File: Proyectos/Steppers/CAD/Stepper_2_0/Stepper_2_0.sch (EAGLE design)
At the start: 4 parts

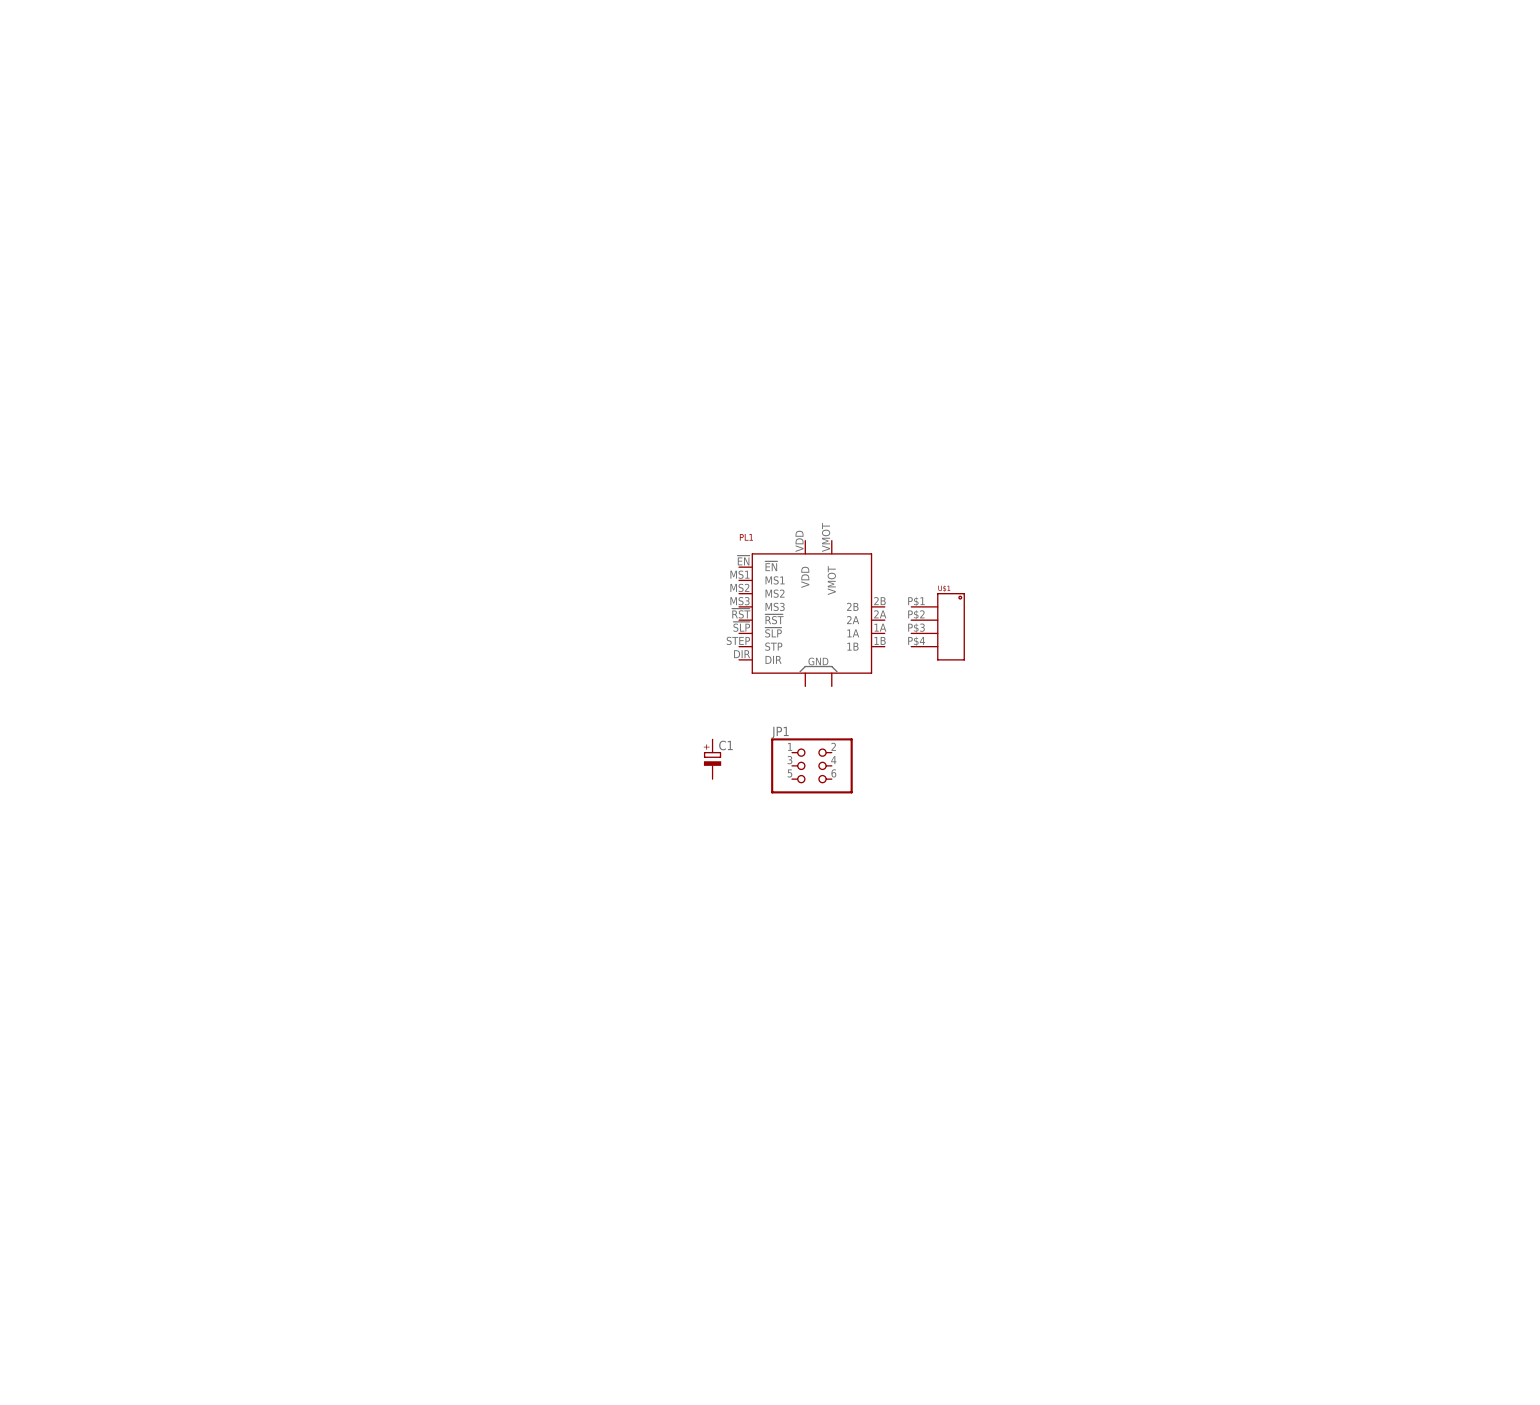
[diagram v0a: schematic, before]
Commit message: Steppers:
Se comienza a agregar el potenciómetro a lalibreria del proyecto, se avanza con el esquemático dela V2
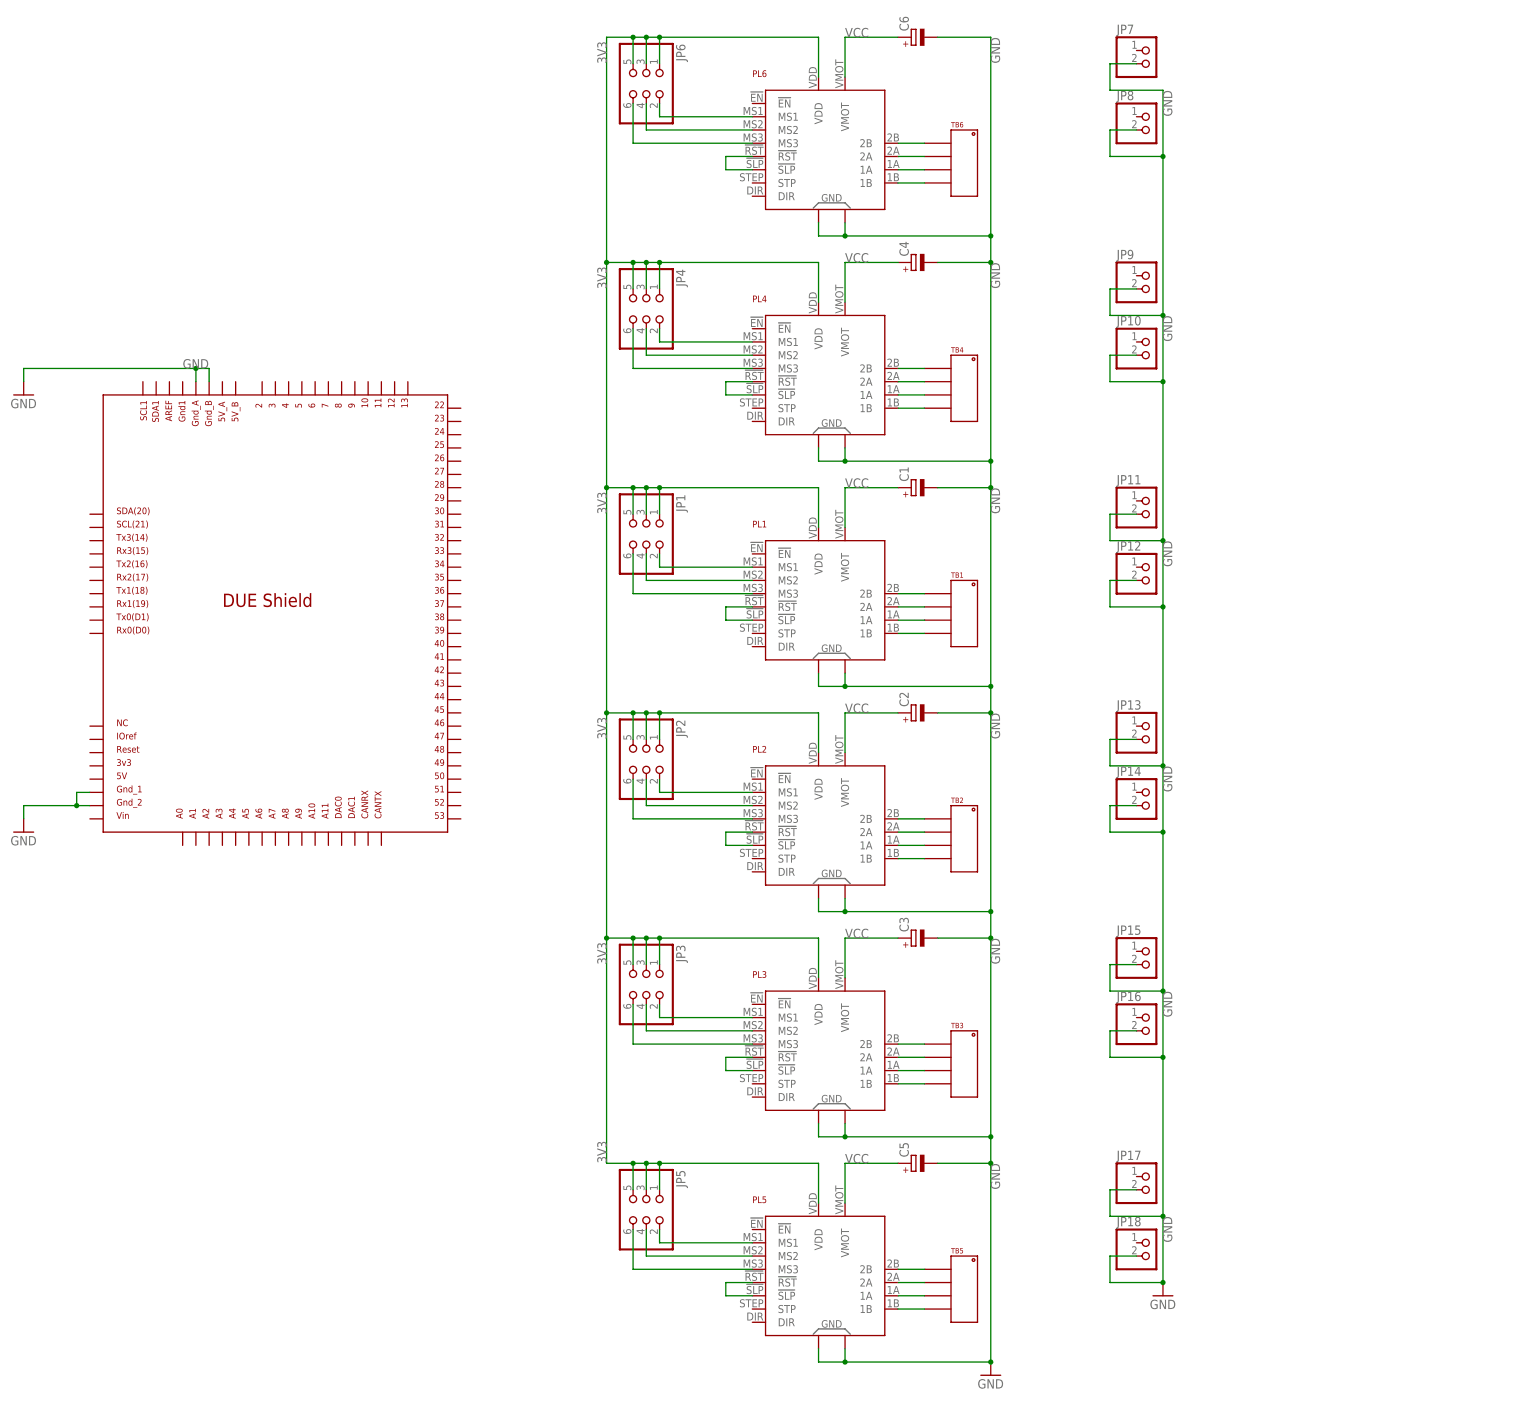
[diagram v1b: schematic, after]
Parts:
- added C2, C3, C4, C5, C6: (no value), rcl:CPOL-EUETR2
- added JP10, JP11, JP12, JP13, JP14, JP15, JP16, JP17, JP18, JP7, JP8, JP9: (no value), pinhead:PINHD-1X2
- added JP2, JP3, JP4, JP5, JP6: (no value), pinhead:PINHD-2X3
- added PL2, PL3, PL4, PL5, PL6: A4988X, Steppers:A4988X
- added TB1, TB2, TB3, TB4, TB5, TB6: TB_HEAD_3.5MM_01X04, Steppers:TB_HEAD_3.5MM_01X04
- U$1: value TB_HEAD_3.5MM_01X04 -> DUE(NOSPI); device Steppers:TB_HEAD_3.5MM_01X04 -> JoshParts:DUE(NOSPI)
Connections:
- new net 3V3: JP1.1, JP1.3, JP1.5, JP2.1, JP2.3, JP2.5, JP3.1, JP3.3, JP3.5, JP4.1, JP4.3, JP4.5, JP5.1, JP5.3, JP5.5, JP6.1, JP6.3, JP6.5, PL1.VDD, PL2.VDD, PL3.VDD, PL4.VDD, PL5.VDD, PL6.VDD
- new net GND: C1.-, C2.-, C3.-, C4.-, C5.-, C6.-, JP10.2, JP11.2, JP12.2, JP13.2, JP14.2, JP15.2, JP16.2, JP17.2, JP18.2, JP7.2, JP8.2, JP9.2, PL1.GND1, PL1.GND2, PL2.GND1, PL2.GND2, PL3.GND1, PL3.GND2, PL4.GND1, PL4.GND2, PL5.GND1, PL5.GND2, PL6.GND1, PL6.GND2, U$1.GND_1, U$1.GND_2, U$1.GND_A, U$1.GND_B
- new net N$1: PL1.1B, TB1.P$4
- new net N$11: PL1.!RST, PL1.!SLP
- new net N$13: PL2.1B, TB2.P$4
- new net N$14: PL2.1A, TB2.P$3
- new net N$15: PL2.2A, TB2.P$2
- new net N$16: PL2.2B, TB2.P$1
- new net N$18: PL2.!RST, PL2.!SLP
- new net N$2: PL1.1A, TB1.P$3
- new net N$20: JP2.6, PL2.MS3
- new net N$21: JP2.4, PL2.MS2
- new net N$22: JP2.2, PL2.MS1
- new net N$24: PL3.1B, TB3.P$4
- new net N$25: PL3.1A, TB3.P$3
- new net N$26: PL3.2A, TB3.P$2
- new net N$27: PL3.2B, TB3.P$1
- new net N$29: PL3.!RST, PL3.!SLP
- new net N$3: PL1.2A, TB1.P$2
- new net N$31: JP3.6, PL3.MS3
- new net N$32: JP3.4, PL3.MS2
- new net N$33: JP3.2, PL3.MS1
- new net N$35: PL4.1B, TB4.P$4
- new net N$36: PL4.1A, TB4.P$3
- new net N$37: PL4.2A, TB4.P$2
- new net N$38: PL4.2B, TB4.P$1
- new net N$4: PL1.2B, TB1.P$1
- new net N$40: PL4.!RST, PL4.!SLP
- new net N$42: JP4.6, PL4.MS3
- new net N$43: JP4.4, PL4.MS2
- new net N$44: JP4.2, PL4.MS1
- new net N$46: PL5.1B, TB5.P$4
- new net N$47: PL5.1A, TB5.P$3
- new net N$48: PL5.2A, TB5.P$2
- new net N$49: PL5.2B, TB5.P$1
- new net N$5: JP1.6, PL1.MS3
- new net N$51: PL5.!RST, PL5.!SLP
- new net N$53: JP5.6, PL5.MS3
- new net N$54: JP5.4, PL5.MS2
- new net N$55: JP5.2, PL5.MS1
- new net N$57: PL6.1B, TB6.P$4
- new net N$58: PL6.1A, TB6.P$3
- new net N$59: PL6.2A, TB6.P$2
- new net N$6: JP1.4, PL1.MS2
- new net N$60: PL6.2B, TB6.P$1
- new net N$62: PL6.!RST, PL6.!SLP
- new net N$64: JP6.6, PL6.MS3
- new net N$65: JP6.4, PL6.MS2
- new net N$66: JP6.2, PL6.MS1
- new net N$7: JP1.2, PL1.MS1
- new net VCC: C1.+, C2.+, C3.+, C4.+, C5.+, C6.+, PL1.VMOT, PL2.VMOT, PL3.VMOT, PL4.VMOT, PL5.VMOT, PL6.VMOT
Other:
- moved on the sheet: C1, JP1, PL1

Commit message: Steppers:
Se mejora el modelo del potenciómetro en la libreria y se agrega l boton de 6mm, se avanza en el esquemático de la V2
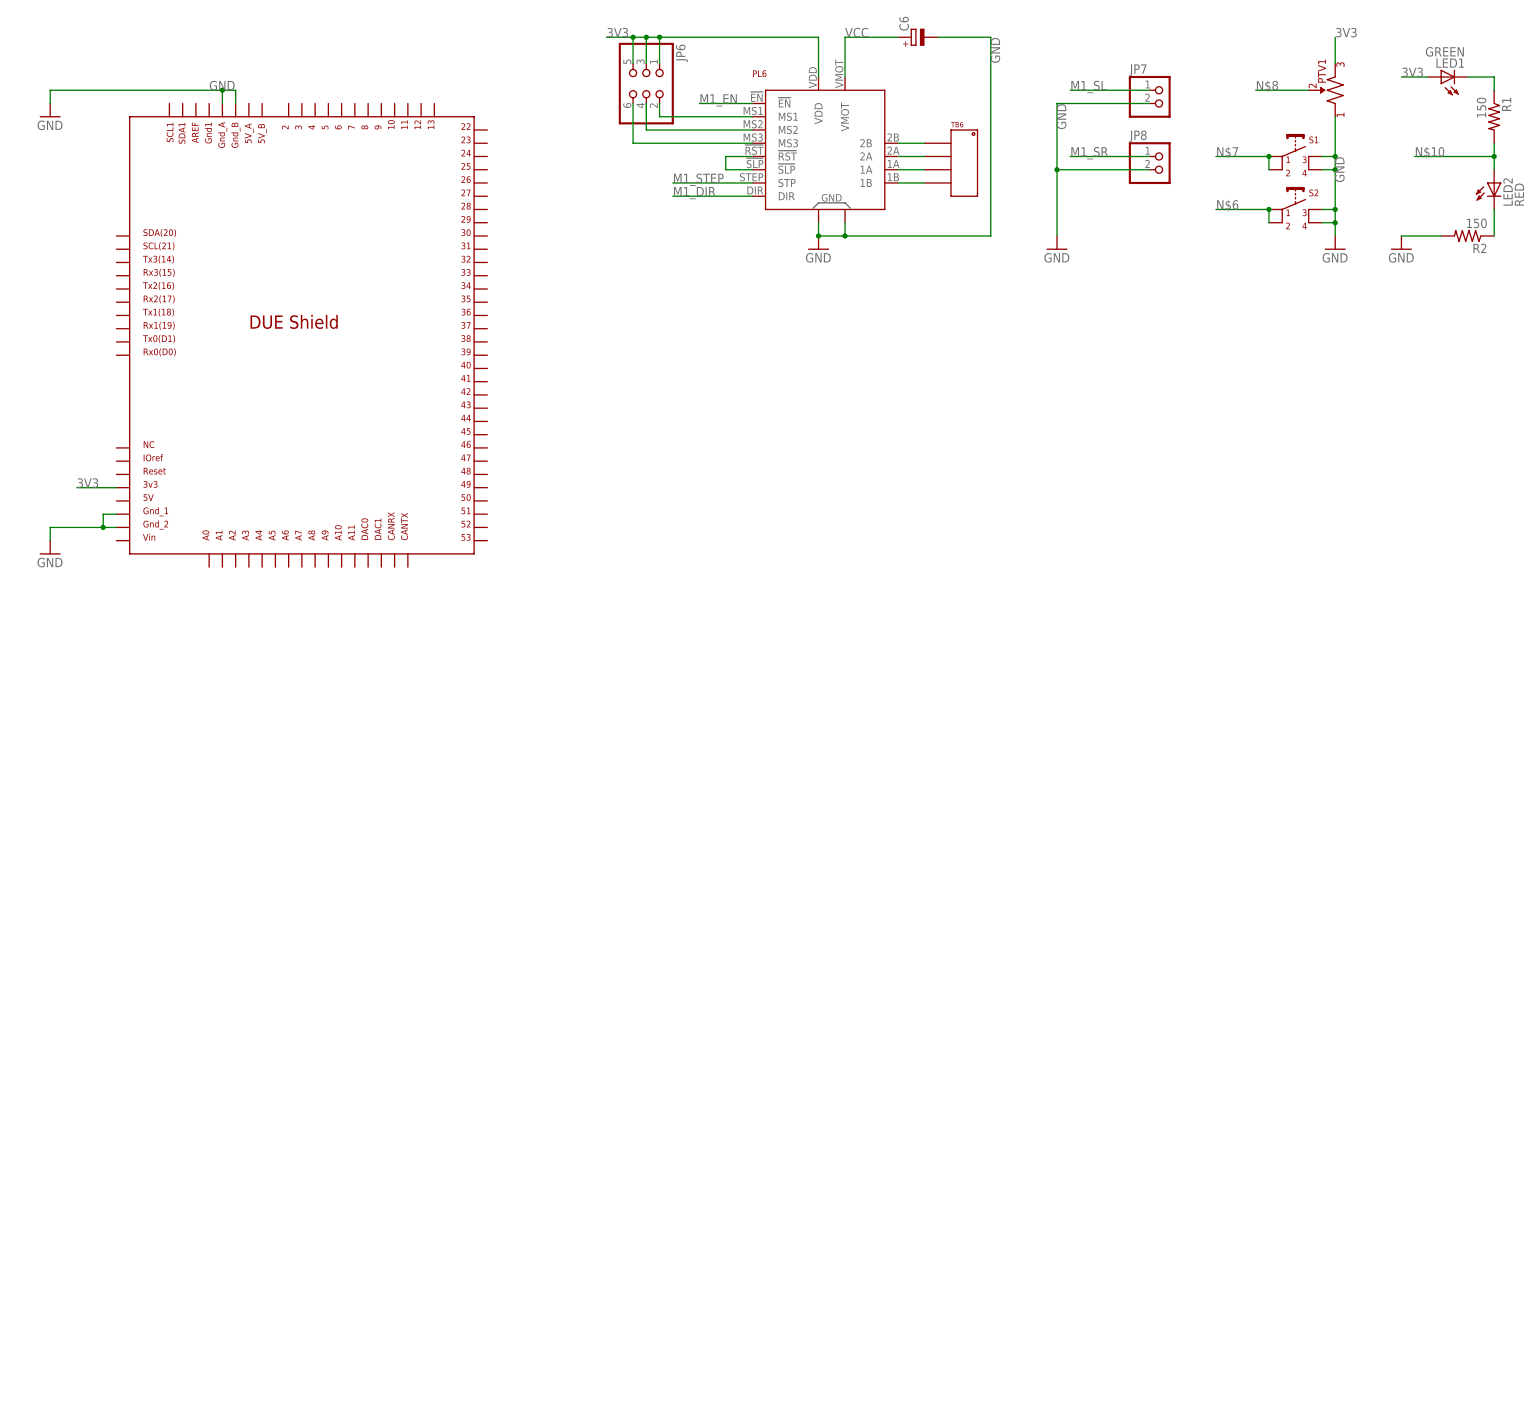
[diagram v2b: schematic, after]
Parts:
- removed C1, C2, C3, C4, C5: (no value), rcl:CPOL-EUETR2
- removed JP1, JP2, JP3, JP4, JP5: (no value), pinhead:PINHD-2X3
- removed JP10, JP11, JP12, JP13, JP14, JP15, JP16, JP17, JP18, JP9: (no value), pinhead:PINHD-1X2
- removed PL1, PL2, PL3, PL4, PL5: A4988X, Steppers:A4988X
- removed TB1, TB2, TB3, TB4, TB5: TB_HEAD_3.5MM_01X04, Steppers:TB_HEAD_3.5MM_01X04
- added LED1: GREEN, adafruit:LEDSMT1206
- added LED2: RED, adafruit:LEDSMT1206
- added PTV1: PTV09A-4, Steppers:PTV09A-4
- added R1, R2: 150, SparkFun-Resistors:RESISTOR1206
- added S1, S2: BTN_SPST_6MM, Steppers:BTN_SPST_6MM
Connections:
- removed net N$1: PL1.1B, TB1.P$4
- removed net N$13: PL2.1B, TB2.P$4
- removed net N$14: PL2.1A, TB2.P$3
- removed net N$15: PL2.2A, TB2.P$2
- removed net N$16: PL2.2B, TB2.P$1
- removed net N$18: PL2.!RST, PL2.!SLP
- removed net N$2: PL1.1A, TB1.P$3
- removed net N$20: JP2.6, PL2.MS3
- removed net N$21: JP2.4, PL2.MS2
- removed net N$22: JP2.2, PL2.MS1
- removed net N$24: PL3.1B, TB3.P$4
- removed net N$25: PL3.1A, TB3.P$3
- removed net N$26: PL3.2A, TB3.P$2
- removed net N$27: PL3.2B, TB3.P$1
- removed net N$29: PL3.!RST, PL3.!SLP
- removed net N$3: PL1.2A, TB1.P$2
- removed net N$31: JP3.6, PL3.MS3
- removed net N$32: JP3.4, PL3.MS2
- removed net N$33: JP3.2, PL3.MS1
- removed net N$35: PL4.1B, TB4.P$4
- removed net N$36: PL4.1A, TB4.P$3
- removed net N$37: PL4.2A, TB4.P$2
- removed net N$38: PL4.2B, TB4.P$1
- removed net N$4: PL1.2B, TB1.P$1
- removed net N$40: PL4.!RST, PL4.!SLP
- removed net N$42: JP4.6, PL4.MS3
- removed net N$43: JP4.4, PL4.MS2
- removed net N$44: JP4.2, PL4.MS1
- removed net N$46: PL5.1B, TB5.P$4
- removed net N$47: PL5.1A, TB5.P$3
- removed net N$48: PL5.2A, TB5.P$2
- removed net N$49: PL5.2B, TB5.P$1
- removed net N$5: JP1.6, PL1.MS3
- removed net N$51: PL5.!RST, PL5.!SLP
- removed net N$53: JP5.6, PL5.MS3
- removed net N$54: JP5.4, PL5.MS2
- removed net N$55: JP5.2, PL5.MS1
- new net M1_DIR: PL6.DIR
- new net M1_EN: PL6.!EN
- new net M1_SL: JP7.1
- new net M1_SR: JP8.1
- new net M1_STEP: PL6.STP
- new net N$10: LED2.A, R1.2
- new net N$12: LED1.A
- new net N$8: PTV1.2
- new net N$9: LED2.C, R2.1
- net 3V3: now also PTV1.3, U$1.3V3; no longer JP1.1, JP1.3, JP1.5, JP2.1, JP2.3, JP2.5, JP3.1, JP3.3, JP3.5, JP4.1, JP4.3, JP4.5, JP5.1, JP5.3, JP5.5, PL1.VDD, PL2.VDD, PL3.VDD, PL4.VDD, PL5.VDD
- net GND: now also PTV1.1, R2.2, S1.3, S1.4, S2.3, S2.4; no longer C1.-, C2.-, C3.-, C4.-, C5.-, JP10.2, JP11.2, JP12.2, JP13.2, JP14.2, JP15.2, JP16.2, JP17.2, JP18.2, JP9.2, PL1.GND1, PL1.GND2, PL2.GND1, PL2.GND2, PL3.GND1, PL3.GND2, PL4.GND1, PL4.GND2, PL5.GND1, PL5.GND2
- net N$11: now also LED1.C, R1.1; no longer PL1.!RST, PL1.!SLP
- net N$6: now also S2.1, S2.2; no longer JP1.4, PL1.MS2
- net N$7: now also S1.1, S1.2; no longer JP1.2, PL1.MS1
- net VCC: no longer C1.+, C2.+, C3.+, C4.+, C5.+, PL1.VMOT, PL2.VMOT, PL3.VMOT, PL4.VMOT, PL5.VMOT
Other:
- moved on the sheet: JP7, JP8
